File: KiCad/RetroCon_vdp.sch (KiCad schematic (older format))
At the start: 64 parts, among them IC1 BH7236, IC21 4464, IC22 4464, IC23 4464, IC24 4464, J10 DIN8_SEL2, J11 DIN8_SEL4, J12 RGB, J14 DIN8_SEL1, J2 SVideo, J4 DIN8_SEL3, J5 MONO, J8 DIN8_SEL5, Q2 21M47727, X2 RAUDIO, X5 LAUDIO, X9 COMPOSITE

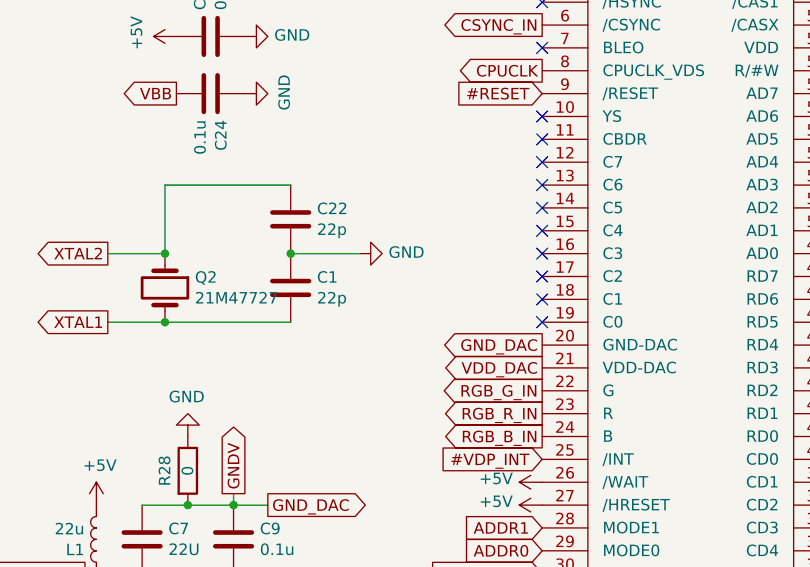
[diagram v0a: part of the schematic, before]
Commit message: Fix up some bugs
fix up around XTAL and add variable capacitor.
fix the position of Joystick ports.
fix +5V supply around DC2DC.
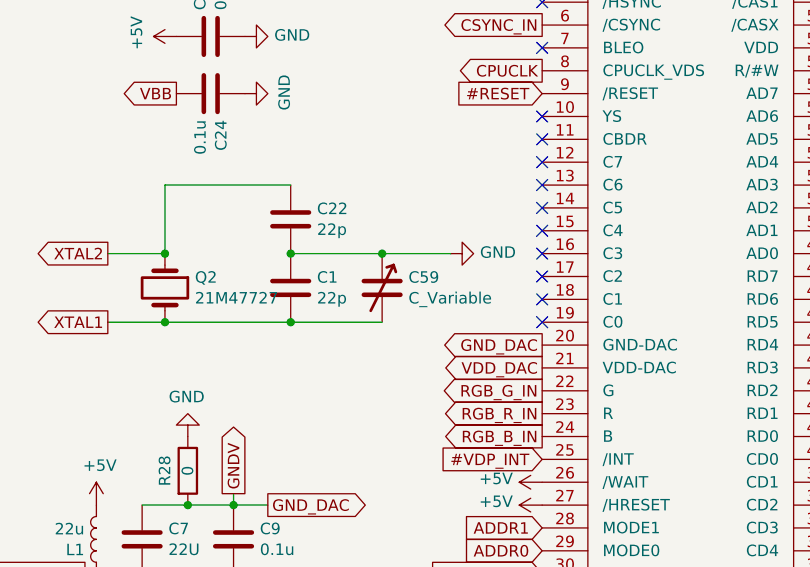
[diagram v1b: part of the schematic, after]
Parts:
- added C59: C_Variable, Capacitor_THT:C_Rect_L7.0mm_W6.5mm_P5.00mm, symbol Device:C_Variable
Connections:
- net GND: now also C59.1
- net XTAL1: now also C59.2
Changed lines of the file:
@@
 Wire Wire Line
 	900  2450 1150 2450
-$Comp
-L Device:C C1
-U 1 1 5DE2CA88
-P 1700 2600
-F 0 "C1" H 1815 2646 50  0000 L CNN
-F 1 "22p" H 1815 2555 50  0000 L CNN
-F 2 "Capacitor_SMD:C_0805_2012Metric_Pad1.15x1.40mm_HandSolder" H 1738 2450 50  0001 C CNN
-F 3 "~" H 1700 2600 50  0001 C CNN
-	1    1700 2600
-	1    0    0    -1
-$EndComp
 Wire Wire Line
 	1150 2150 1150 2450
 Connection ~ 1150 2450
-Wire Wire Line
-	1700 2450 2000 2450
 $Comp
 L power:GND #PWR0128
 U 1 1 5DE31365
-P 2000 2450
-F 0 "#PWR0128" H 2000 2200 50  0001 C CNN
-F 1 "GND" V 2005 2322 50  0000 R CNN
-F 2 "" H 2000 2450 50  0001 C CNN
-F 3 "" H 2000 2450 50  0001 C CNN
-	1    2000 2450
+P 2400 2450
+F 0 "#PWR0128" H 2400 2200 50  0001 C CNN
+F 1 "GND" V 2405 2322 50  0000 R CNN
+F 2 "" H 2400 2450 50  0001 C CNN
+F 3 "" H 2400 2450 50  0001 C CNN
+	1    2400 2450
 	0    -1   -1   0
 $EndComp
@@
 	1    0    0    -1
 $EndComp
-Connection ~ 1700 2450
 Text GLabel 5500 3000 0    50   Input ~ 0
 GNDV
@@
 Text GLabel 8350 5100 1    50   Input ~ 0
 GNDV
+$Comp
+L Device:C_Variable C59
+U 1 1 5E92B413
+P 2100 2600
+F 0 "C59" H 2215 2646 50  0000 L CNN
+F 1 "C_Variable" H 2215 2555 50  0000 L CNN
+F 2 "Capacitor_THT:C_Rect_L7.0mm_W6.5mm_P5.00mm" H 2100 2600 50  0001 C CNN
+F 3 "~" H 2100 2600 50  0001 C CNN
+	1    2100 2600
+	1    0    0    -1
+$EndComp
+Connection ~ 1700 2450
+$Comp
+L Device:C C1
+U 1 1 5DE2CA88
+P 1700 2600
+F 0 "C1" H 1815 2646 50  0000 L CNN
+F 1 "22p" H 1815 2555 50  0000 L CNN
+F 2 "Capacitor_SMD:C_0805_2012Metric_Pad1.15x1.40mm_HandSolder" H 1738 2450 50  0001 C CNN
+F 3 "~" H 1700 2600 50  0001 C CNN
+	1    1700 2600
+	1    0    0    -1
+$EndComp
+Wire Wire Line
+	2100 2750 1700 2750
+Connection ~ 1700 2750
+Wire Wire Line
+	1700 2450 2100 2450
+Connection ~ 2100 2450
+Wire Wire Line
+	2100 2450 2400 2450
 $EndSCHEMATC

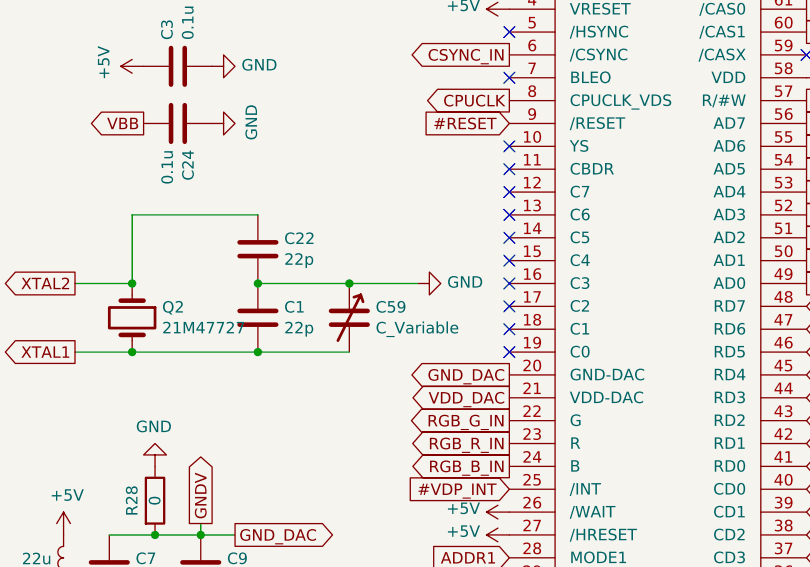
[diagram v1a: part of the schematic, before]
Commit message: fix up some details
change proper value of Capacitor for XTAL
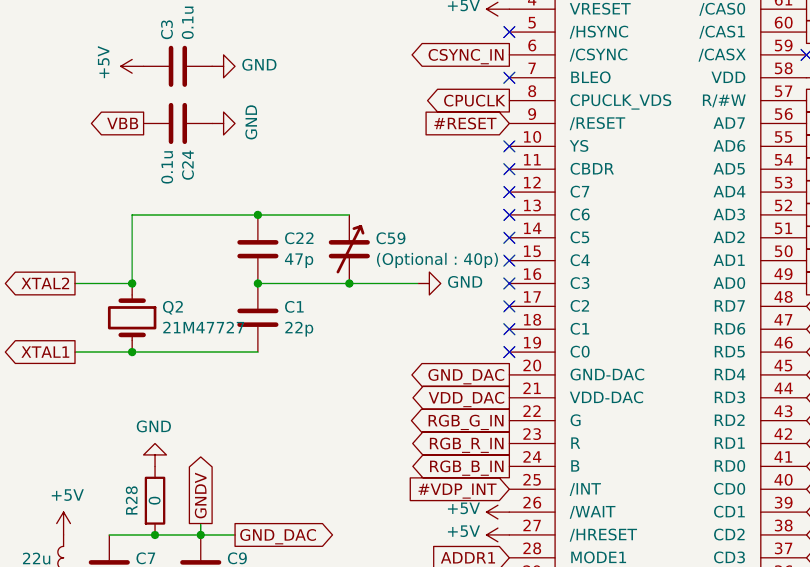
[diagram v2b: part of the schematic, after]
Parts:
- C22: value 22p -> 47p
- C59: value C_Variable -> (Optional : 40p)
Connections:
- net GND: now also C59.2; no longer C59.1
- net XTAL1: no longer C59.2
- net XTAL2: now also C59.1
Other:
- moved on the sheet: C59
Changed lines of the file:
@@
 P 1700 2300
 F 0 "C22" H 1815 2346 50  0000 L CNN
-F 1 "22p" H 1815 2255 50  0000 L CNN
+F 1 "47p" H 1815 2255 50  0000 L CNN
 F 2 "Capacitor_SMD:C_0805_2012Metric_Pad1.15x1.40mm_HandSolder" H 1738 2150 50  0001 C CNN
 F 3 "~" H 1700 2300 50  0001 C CNN
@@
 L Device:C_Variable C59
 U 1 1 5E92B413
-P 2100 2600
-F 0 "C59" H 2215 2646 50  0000 L CNN
-F 1 "C_Variable" H 2215 2555 50  0000 L CNN
-F 2 "Capacitor_THT:C_Rect_L7.0mm_W6.5mm_P5.00mm" H 2100 2600 50  0001 C CNN
-F 3 "~" H 2100 2600 50  0001 C CNN
-	1    2100 2600
+P 2100 2300
+F 0 "C59" H 2215 2346 50  0000 L CNN
+F 1 "(Optional : 40p)" H 2215 2255 50  0000 L CNN
+F 2 "Capacitor_THT:C_Rect_L7.0mm_W6.5mm_P5.00mm" H 2100 2300 50  0001 C CNN
+F 3 "~" H 2100 2300 50  0001 C CNN
+	1    2100 2300
 	1    0    0    -1
 $EndComp
@@
 $EndComp
 Wire Wire Line
-	2100 2750 1700 2750
-Connection ~ 1700 2750
-Wire Wire Line
 	1700 2450 2100 2450
 Connection ~ 2100 2450
 Wire Wire Line
 	2100 2450 2400 2450
+Wire Wire Line
+	2100 2150 1700 2150
+Connection ~ 1700 2150
 $EndSCHEMATC
